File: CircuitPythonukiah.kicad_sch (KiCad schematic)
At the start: 23 parts, among them J1 USB_B_Micro, SW1 SW_DIP_x01, SW2 SW_DIP_x01, U1 TinyS2

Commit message: Add KiCAD files
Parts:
- U1: symbol Unexpected Maker:TinyS2 -> CircuitPythonukiah:TinyS2
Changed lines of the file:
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@@
     (pin "2")
   )
-  (symbol (lib_id "Unexpected Maker:TinyS2") (at 68.58 172.72 0) (unit 1)
+  (symbol (lib_id "CircuitPythonukiah:TinyS2") (at 68.58 172.72 0) (unit 1)
     (in_bom yes) (on_board yes) (fields_autoplaced)
     (property "Reference" "U1" (id 0) (at 69.215 152.4 0))

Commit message: Update repo with currnt work
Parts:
- removed SW2: SW_DIP_x01, Button_Switch_SMD:SW_DIP_SPSTx01_Slide_6.7x4.1mm_W8.61mm_P2.54mm_LowProfile, symbol Switch:SW_DIP_x01
- removed U1: TinyS2, Unexpected Maker:TinyS2, symbol CircuitPythonukiah:TinyS2
- added U1: QT_Py, Adafruit:QT Py, symbol Adafruit:QT_Py
- J1: footprint Connector_USB:USB_Micro-B_Wuerth_614105150721_Vertical_CircularHoles -> CUI Devices:CUI_UJC-VP-3-SMT-TR; symbol Connector:USB_B_Micro -> CUI Devices:UJC-VP-3-SMT-TR; MANUFACTURER (none) -> CUI Devices; MAXIMUM_PACKAGE_HEIGHT (none) -> 6.5mm; PARTREV (none) -> 1.0; STANDARD (none) -> Manufacturer Recommendations
- R1, R2, R3, R4, R5, R6, R7, R8, R9: value 10K -> 100; footprint Resistor_SMD:R_0805_2012Metric_Pad1.20x1.40mm_HandSolder -> Resistor_THT:R_Axial_DIN0207_L6.3mm_D2.5mm_P7.62mm_Horizontal
- SW1: footprint Button_Switch_SMD:SW_DIP_SPSTx01_Slide_6.7x4.1mm_W8.61mm_P2.54mm_LowProfile -> E-Switch:EG1218; symbol Switch:SW_DIP_x01 -> Switch:SW_SPDT; MANUFACTURER (none) -> CW Industries; MAXIMUM_PACKAGE_HIEGHT (none) -> 14.96 mm; PARTREV (none) -> May 20, 2003; STANDARD (none) -> Manufacturer Recommendations
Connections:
- net 3V: now also SW1.2 (B), U1.3 (3V); no longer SW1.1
- net 5V: now also J1.A9 (VBUS), J1.B9 (VBUS), U1.1 (5V); no longer J1.1 (VBUS)
- net GND: now also J1.A12 (GND), J1.B12 (GND), J1.S1 (SHIELD), J1.S2 (SHIELD), U1.2 (GND); no longer J1.5 (GND), J1.6 (Shield)
- net LED1: now also U1.7 (RX)
- net LED2: now also U1.6 (SCK)
- net LED3: now also U1.5 (MI)
- net LED4: now also U1.4 (MO)
- net LED5: now also U1.11 (A3)
- net LED6: now also U1.12 (SDA)
- net LED7: now also U1.13 (SCL)
- net LED8: now also U1.14 (TX)
- net MUTE_BTN: now also SW1.1 (A), U1.9 (A1); no longer SW1.2
- net SHAMASH: now also U1.10 (A2)
- net SPKR: now also U1.8 (A0)

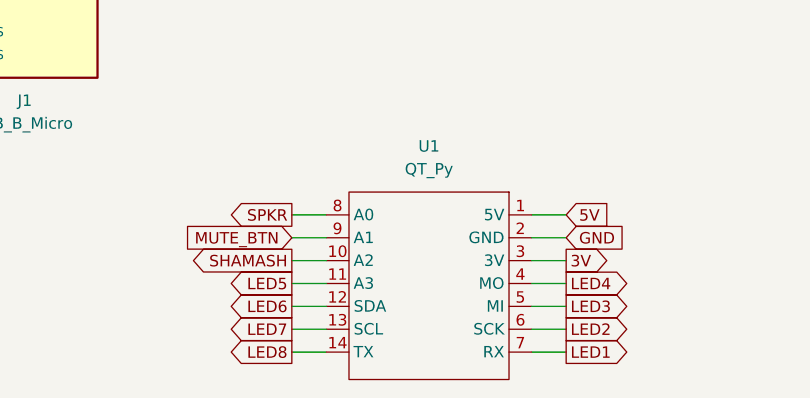
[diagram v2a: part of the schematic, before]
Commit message: Flip microcontroller for ease of configuring
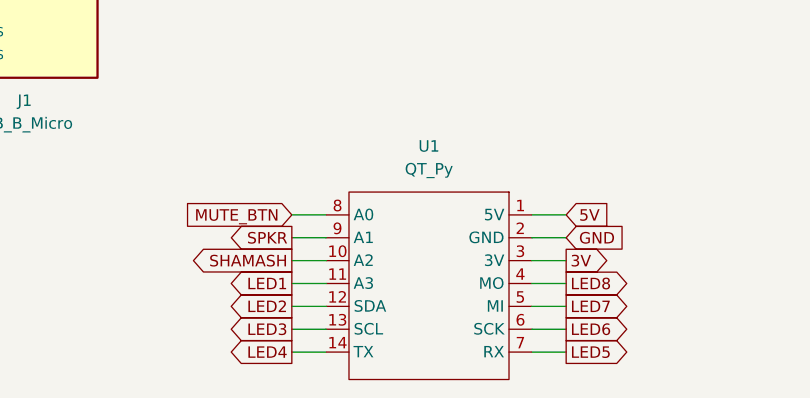
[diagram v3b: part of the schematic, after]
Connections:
- net LED1: now also U1.11 (A3); no longer U1.7 (RX)
- net LED2: now also U1.12 (SDA); no longer U1.6 (SCK)
- net LED3: now also U1.13 (SCL); no longer U1.5 (MI)
- net LED4: now also U1.14 (TX); no longer U1.4 (MO)
- net LED5: now also U1.7 (RX); no longer U1.11 (A3)
- net LED6: now also U1.6 (SCK); no longer U1.12 (SDA)
- net LED7: now also U1.5 (MI); no longer U1.13 (SCL)
- net LED8: now also U1.4 (MO); no longer U1.14 (TX)
- net MUTE_BTN: now also U1.8 (A0); no longer U1.9 (A1)
- net SPKR: now also U1.9 (A1); no longer U1.8 (A0)

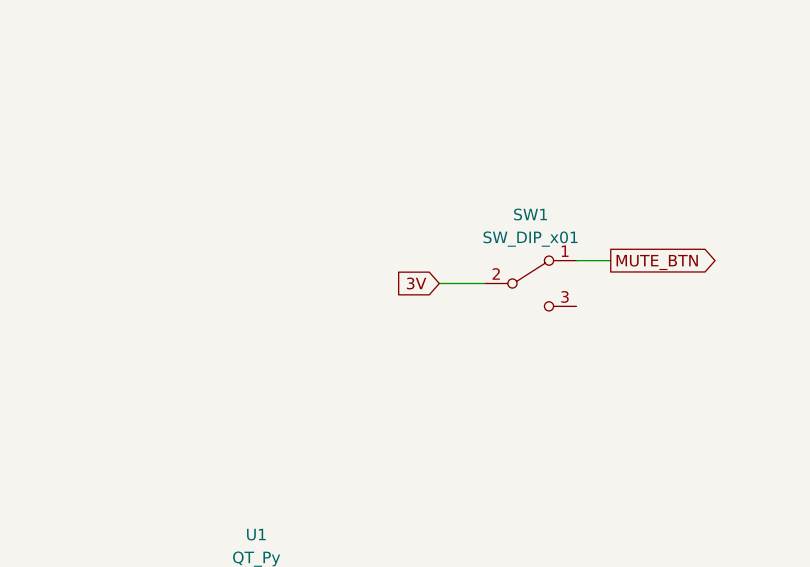
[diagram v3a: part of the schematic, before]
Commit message: Change A0 to be pull-up input
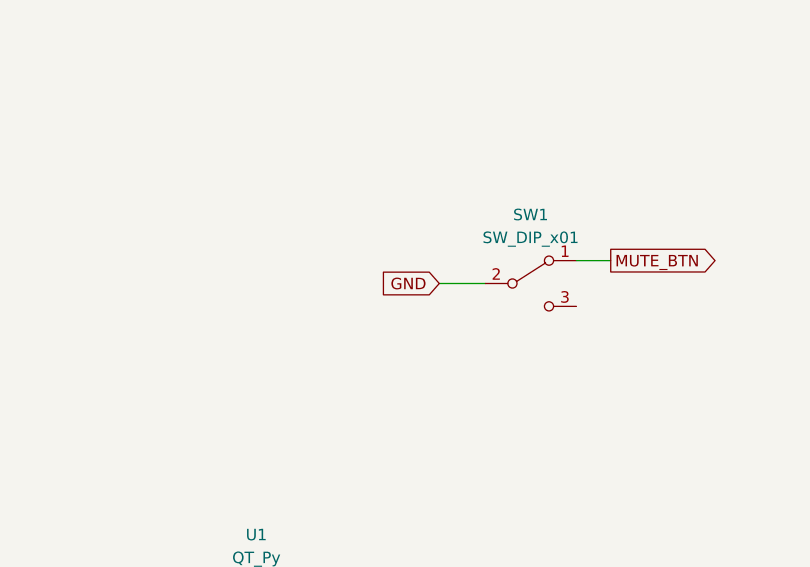
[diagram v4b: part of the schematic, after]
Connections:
- net 3V: no longer SW1.2 (B)
- net GND: now also SW1.2 (B)
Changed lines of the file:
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@@
     )
   )
-  (global_label "3V" (shape input) (at 135.89 107.95 180) (fields_autoplaced)
+  (global_label "GND" (shape input) (at 135.89 107.95 180) (fields_autoplaced)
     (effects (font (size 1.27 1.27)) (justify right))
-    (property "Intersheet References" "${INTERSHEET_REFS}" (id 0) (at 131.1788 107.8706 0)
+    (property "Intersheet References" "${INTERSHEET_REFS}" (id 0) (at 129.6064 107.8706 0)
       (effects (font (size 1.27 1.27)) (justify right) hide)
     )
